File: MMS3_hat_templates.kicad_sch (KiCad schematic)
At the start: 12 parts, among them U4 AMS1117

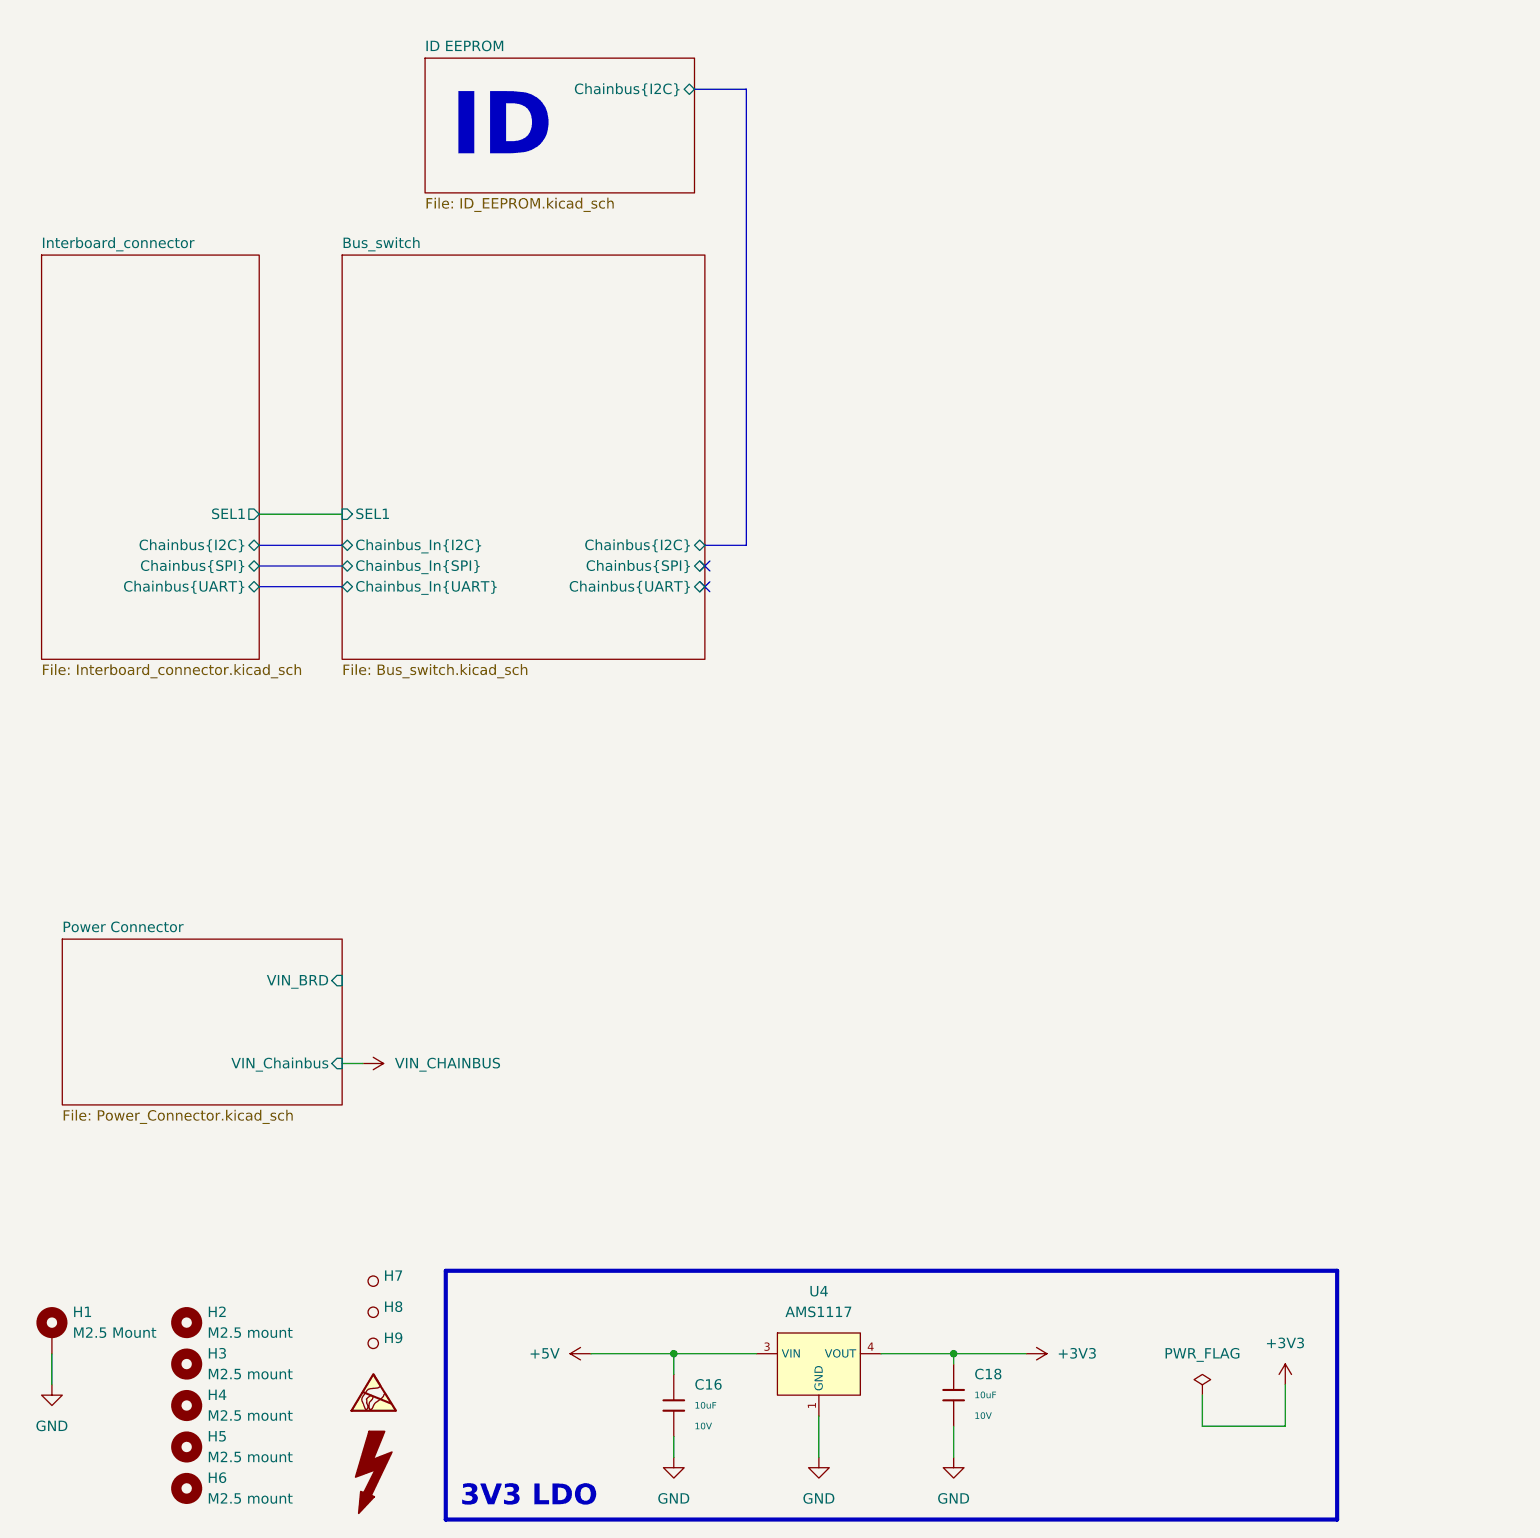
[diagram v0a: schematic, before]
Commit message: added box around chainbus bus switch in schematic
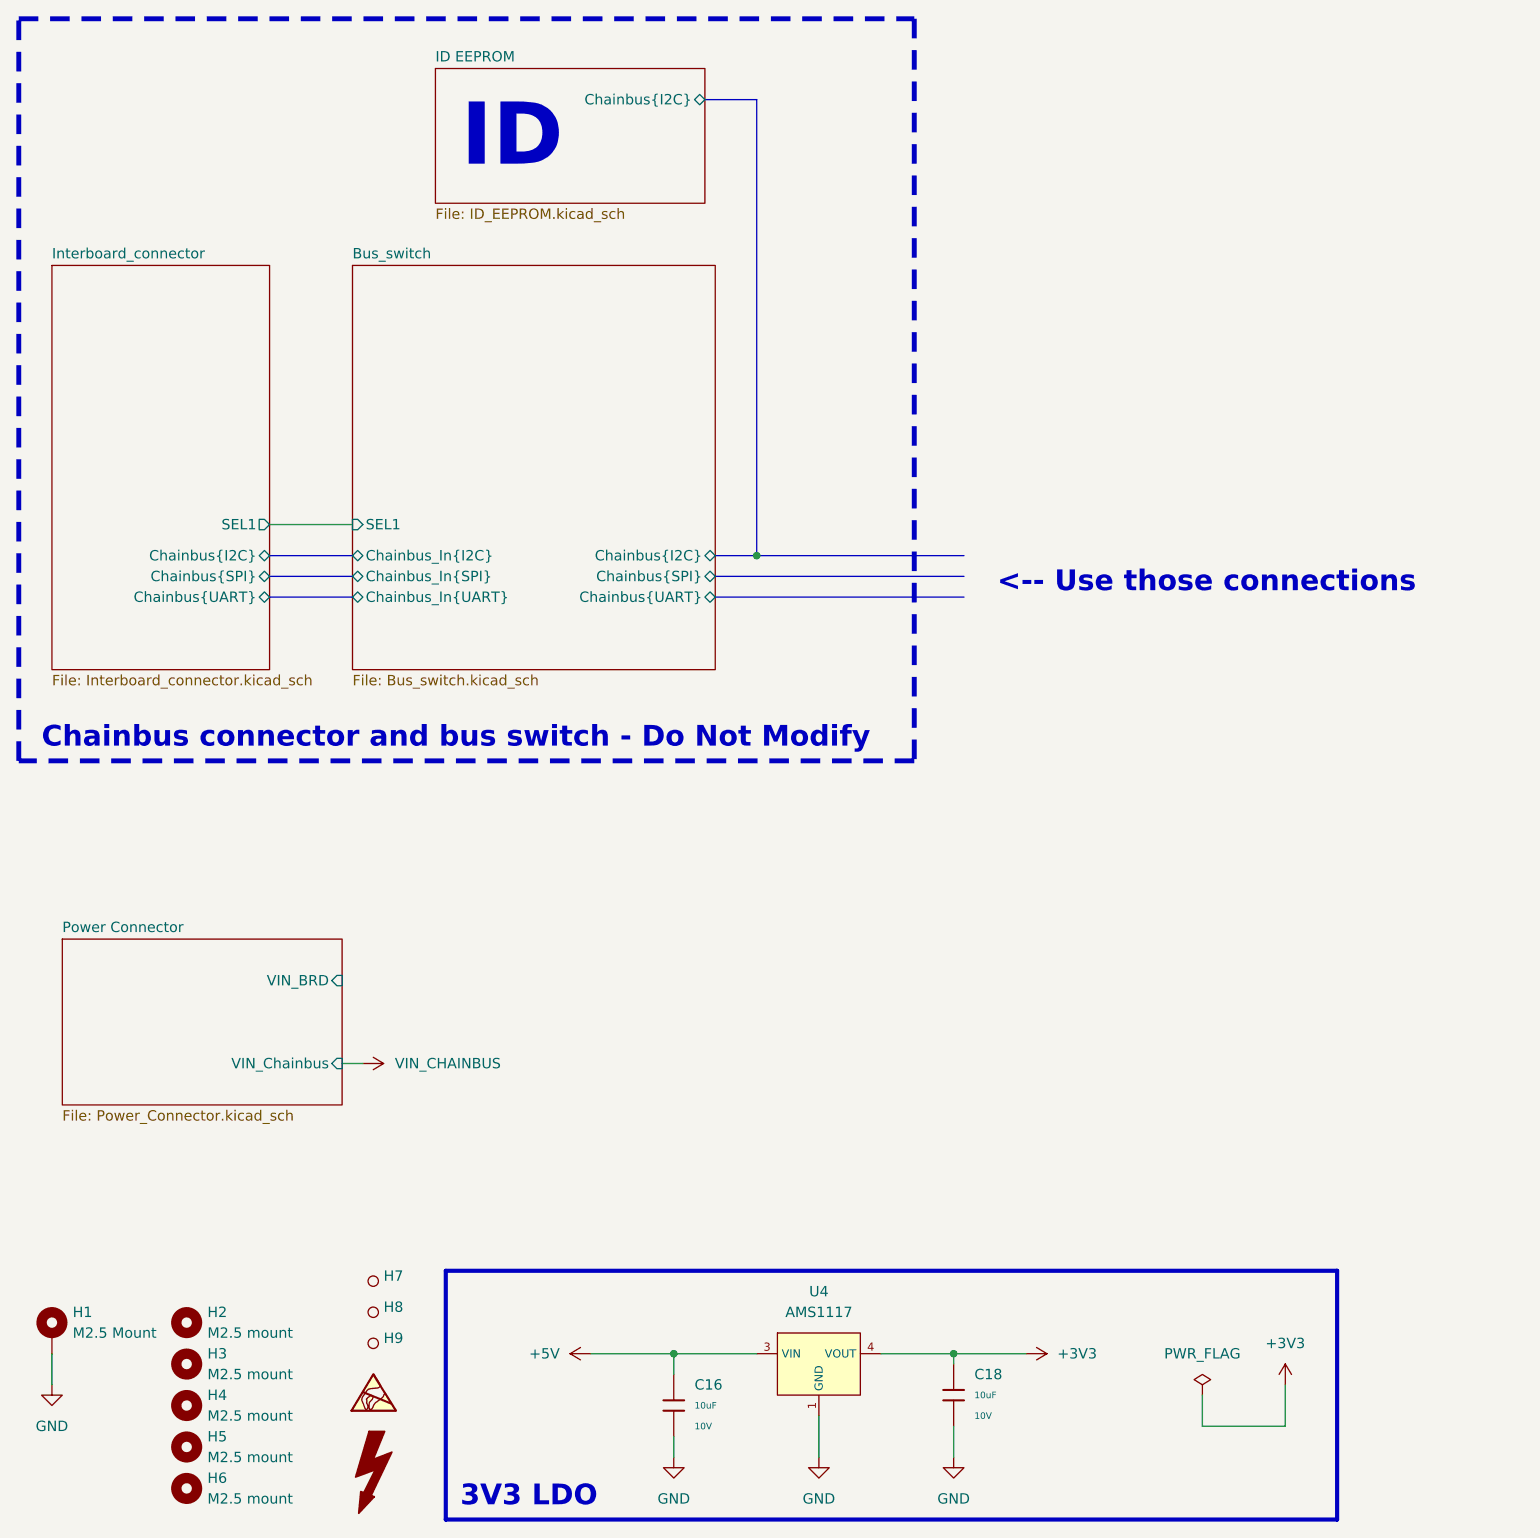
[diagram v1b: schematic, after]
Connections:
- no-connect marks 2 -> 0
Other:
- note added: "<-- Use those connections"
- note added: "Chainbus connector and bus switch - Do Not Modify"
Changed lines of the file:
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@@
 	)
 	(rectangle
+		(start 12.446 12.954)
+		(end 122.174 103.886)
+		(stroke
+			(width 0.6)
+			(type dash)
+			(color 132 0 0 1)
+		)
+		(fill
+			(type none)
+		)
+	)
+	(rectangle
 		(start 64.77 166.37)
 		(end 173.99 196.85)
@@
 		)
 	)
+	(text "<-- Use those connections"
+		(exclude_from_sim no)
+		(at 132.334 82.042 0)
+		(effects
+			(font
+				(size 2.54 2.54)
+				(thickness 0.762)
+				(bold yes)
+			)
+			(justify left)
+		)
+	)
 	(text "ID"
 		(exclude_from_sim no)
-		(at 71.628 26.162 0)
+		(at 72.898 27.432 0)
 		(effects
 			(font
@@
 		)
 	)
+	(text "Chainbus connector and bus switch - Do Not Modify"
+		(exclude_from_sim no)
+		(at 15.24 101.092 0)
+		(effects
+			(font
+				(size 2.54 2.54)
+				(thickness 0.762)
+				(bold yes)
+			)
+			(justify left)
+		)
+	)
+	(junction
+		(at 102.87 78.74)
+		(diameter 0)
+		(color 0 0 0 0)
+	)
 	(junction
 		(at 127 176.53)
@@
 		(color 0 0 0 0)
 	)
-	(no_connect
-		(at 96.52 82.55)
-	)
-	(no_connect
-		(at 96.52 80.01)
-	)
 	(wire
 		(pts
@@
 	(bus
 		(pts
-			(xy 96.52 77.47) (xy 101.6 77.47)
+			(xy 97.79 78.74) (xy 102.87 78.74)
 		)
 		(stroke
@@
 	(bus
 		(pts
-			(xy 101.6 77.47) (xy 101.6 21.59)
+			(xy 102.87 78.74) (xy 102.87 22.86)
 		)
 		(stroke
@@
 	(bus
 		(pts
-			(xy 41.91 82.55) (xy 52.07 82.55)
+			(xy 43.18 83.82) (xy 53.34 83.82)
+		)
+		(stroke
+			(width 0)
+			(type default)
+		)
+	)
+	(bus
+		(pts
+			(xy 97.79 81.28) (xy 128.27 81.28)
 		)
 		(stroke
@@
 		)
 	)
+	(bus
+		(pts
+			(xy 97.79 83.82) (xy 128.27 83.82)
+		)
+		(stroke
+			(width 0)
+			(type default)
+		)
+	)
 	(wire
 		(pts
@@
 	(wire
 		(pts
-			(xy 41.91 73.66) (xy 52.07 73.66)
+			(xy 43.18 74.93) (xy 53.34 74.93)
 		)
 		(stroke
@@
 	(bus
 		(pts
-			(xy 41.91 80.01) (xy 52.07 80.01)
+			(xy 43.18 81.28) (xy 53.34 81.28)
 		)
 		(stroke
@@
 	(bus
 		(pts
-			(xy 101.6 21.59) (xy 95.25 21.59)
+			(xy 102.87 22.86) (xy 96.52 22.86)
 		)
 		(stroke
@@
 	(bus
 		(pts
-			(xy 41.91 77.47) (xy 52.07 77.47)
+			(xy 43.18 78.74) (xy 53.34 78.74)
 		)
 		(stroke
@@
 		)
 	)
+	(bus
+		(pts
+			(xy 102.87 78.74) (xy 128.27 78.74)
+		)
+		(stroke
+			(width 0)
+			(type default)
+		)
+	)
 	(wire
 		(pts
@@
 	)
 	(image
-		(at 74.93 59.69)
+		(at 76.2 60.96)
 		(scale 0.61046)
 		(data "iVBORw0KGgoAAAANSUhEUgAAARAAAACZCAYAAADnwmWxAAAAAXNSR0IArs4c6QAAAARnQU1BAACx"
@@
 	)
 	(image
-		(at 28.493 56.771)
+		(at 29.763 58.041)
 		(scale 0.276586)
 		(data "iVBORw0KGgoAAAANSUhEUgAAA+gAAAPoCAIAAADCwUOzAAAAA3NCSVQICAjb4U/gAAAgAElEQVR4"
@@
 	)
 	(sheet
-		(at 62.23 17.78)
+		(at 63.5 19.05)
 		(size 33.02 16.51)
 		(exclude_from_sim no)
@@
 		)
 		(property "Sheetname" "ID EEPROM"
-			(at 62.23 17.0684 0)
+			(at 63.5 18.3384 0)
 			(show_name no)
 			(do_not_autoplace no)
@@
 		)
 		(property "Sheetfile" "ID_EEPROM.kicad_sch"
-			(at 62.23 34.8746 0)
+			(at 63.5 36.1446 0)
 			(show_name no)
 			(do_not_autoplace no)
@@
 		)
 		(pin "Chainbus{I2C}" bidirectional
-			(at 95.25 21.59 0)
+			(at 96.52 22.86 0)
 			(effects
 				(font
@@
 	)
 	(sheet
-		(at 52.07 41.91)
+		(at 53.34 43.18)
 		(size 44.45 49.53)
 		(exclude_from_sim no)
@@
 		)
 		(property "Sheetname" "Bus_switch"
-			(at 52.07 41.1984 0)
+			(at 53.34 42.4684 0)
 			(show_name no)
 			(do_not_autoplace no)
@@
 		)
 		(property "Sheetfile" "Bus_switch.kicad_sch"
-			(at 52.07 92.0246 0)
+			(at 53.34 93.2946 0)
 			(show_name no)
 			(do_not_autoplace no)
@@
 		)
 		(pin "Chainbus_In{I2C}" bidirectional
-			(at 52.07 77.47 180)
+			(at 53.34 78.74 180)
 			(effects
 				(font
@@
 		)
 		(pin "Chainbus_In{SPI}" bidirectional
-			(at 52.07 80.01 180)
+			(at 53.34 81.28 180)
 			(effects
 				(font
@@
 		)
 		(pin "Chainbus_In{UART}" bidirectional
-			(at 52.07 82.55 180)
+			(at 53.34 83.82 180)
 			(effects
 				(font
@@
 		)
 		(pin "Chainbus{I2C}" bidirectional
-			(at 96.52 77.47 0)
+			(at 97.79 78.74 0)
 			(effects
 				(font
@@
 		)
 		(pin "Chainbus{SPI}" bidirectional
-			(at 96.52 80.01 0)
+			(at 97.79 81.28 0)
 			(effects
 				(font
@@
 		)
 		(pin "Chainbus{UART}" bidirectional
-			(at 96.52 82.55 0)
+			(at 97.79 83.82 0)
 			(effects
 				(font
@@
 		)
 		(pin "SEL1" input
-			(at 52.07 73.66 180)
+			(at 53.34 74.93 180)
 			(effects
 				(font
@@
 	)
 	(sheet
-		(at 15.24 41.91)
+		(at 16.51 43.18)
 		(size 26.67 49.53)
 		(exclude_from_sim no)
@@
 		)
 		(property "Sheetname" "Interboard_connector"
-			(at 15.24 41.1984 0)
+			(at 16.51 42.4684 0)
 			(show_name no)
 			(do_not_autoplace no)
@@
 		)
 		(property "Sheetfile" "Interboard_connector.kicad_sch"
-			(at 15.24 92.0246 0)
+			(at 16.51 93.2946 0)
 			(show_name no)
 			(do_not_autoplace no)
@@
 		)
 		(pin "Chainbus{I2C}" bidirectional
-			(at 41.91 77.47 0)
+			(at 43.18 78.74 0)
 			(effects
 				(font
@@
 		)
 		(pin "Chainbus{SPI}" bidirectional
-			(at 41.91 80.01 0)
+			(at 43.18 81.28 0)
 			(effects
 				(font
@@
 		)
 		(pin "Chainbus{UART}" bidirectional
-			(at 41.91 82.55 0)
+			(at 43.18 83.82 0)
 			(effects
 				(font
@@
 		)
 		(pin "SEL1" output
-			(at 41.91 73.66 0)
+			(at 43.18 74.93 0)
 			(effects
 				(font
